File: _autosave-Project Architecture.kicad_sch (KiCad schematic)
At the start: 4 parts

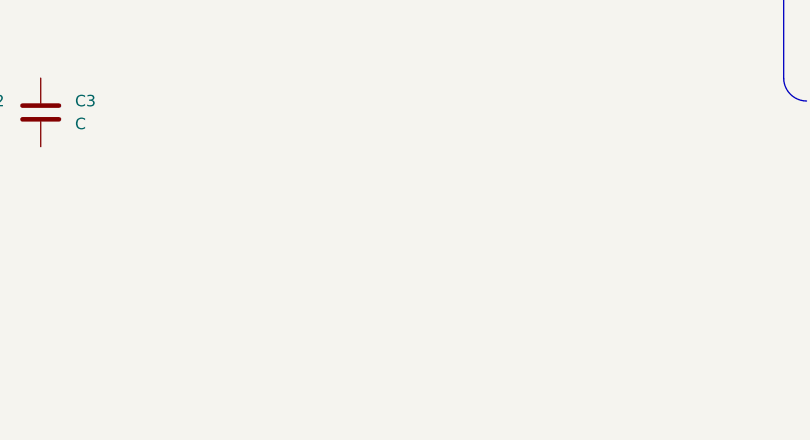
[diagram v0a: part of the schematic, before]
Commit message: CM5 IO done
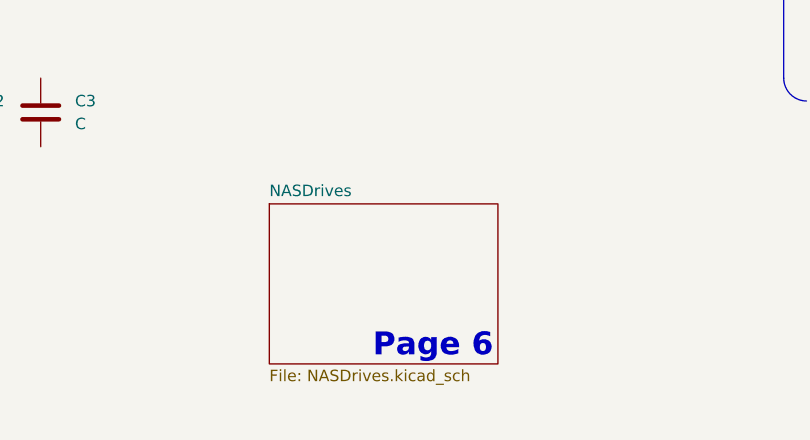
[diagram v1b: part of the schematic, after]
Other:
- added sheet NASDrives (NASDrives.kicad_sch)
- note added: "Page 6"
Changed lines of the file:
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@@
+		)
+	)
+	(text "Page 6"
+		(exclude_from_sim no)
+		(at 163.322 101.092 0)
+		(effects
+			(font
+				(size 2.54 2.54)
+				(bold yes)
+				(color 100 49 70 1)
+			)
+			(justify right bottom)
+			(href "#6")
 		)
 	)
@@
 				)
 			)
+		)
+	)
+	(sheet
+		(at 138.43 83.82)
+		(size 25.4 17.78)
+		(exclude_from_sim no)
+		(in_bom yes)
+		(on_board yes)
+		(dnp no)
+		(fields_autoplaced yes)
+		(stroke
+			(width 0.1524)
+			(type solid)
+		)
+		(fill
+			(color 0 0 0 0.0000)
+		)
+		(property "Sheetname" "NASDrives"
+			(at 138.43 83.1084 0)
+			(effects
+				(font
+					(size 1.27 1.27)
+				)
+				(justify left bottom)
+			)
+		)
+		(property "Sheetfile" "NASDrives.kicad_sch"
+			(at 138.43 102.1846 0)
+			(effects
+				(font
+					(size 1.27 1.27)
+				)
+				(justify left top)
+			)
+		)
+		(instances
+			(project "CM5 Nas"
+				(path "/0650c7a8-acba-429c-9f8e-eec0baf0bc1c/fede4c36-00cc-4d3d-b71c-5243ba232202"
+					(page "6")
+				)
+			)
